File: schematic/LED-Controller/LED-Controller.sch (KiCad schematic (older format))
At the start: 17 parts

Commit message: Schematic first draft
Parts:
- removed J?: Enable Pull-ups, symbol Connector:Conn_01x02_Male
- removed R? (x5): R, symbol Device:R
- added D1: LED, LED_SMD:LED_0603_1608Metric_Pad1.05x0.95mm_HandSolder, symbol Device:LED
- added J10: String6, Connector_Wire:SolderWire-1sqmm_1x03_P7.8mm_D1.4mm_OD3.9mm, symbol Connector:Conn_01x03_Male
- added J3: RCin, Connector_PinHeader_2.54mm:PinHeader_1x03_P2.54mm_Horizontal, symbol Connector:Conn_01x03_Male
- added R1: 220, Resistor_SMD:R_0603_1608Metric, symbol Device:R
- added R2: 10k, Resistor_SMD:R_0603_1608Metric, symbol Device:R
- C1: renamed from C?; footprint (none) -> Capacitor_SMD:C_1206_3216Metric_Pad1.33x1.80mm_HandSolder
- C2: renamed from C?; value C -> 0.1 uF; footprint (none) -> Capacitor_SMD:C_0603_1608Metric_Pad1.08x0.95mm_HandSolder
- J1: renamed from J?; footprint (none) -> Connector_Wire:SolderWire-2.5sqmm_1x02_P8.8mm_D2.4mm_OD4.4mm
- J4: renamed from J?; footprint (none) -> Connector_PinHeader_2.54mm:PinHeader_1x03_P2.54mm_Vertical
- J5, J6, J7, J8, J9: renamed from J?; footprint (none) -> Connector_Wire:SolderWire-1sqmm_1x03_P7.8mm_D1.4mm_OD3.9mm
- U1: renamed from U?; value PIC18F26K22-xSO -> PIC18F27Q43-xSO
- gave numbers to parts that had none: 1
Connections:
- net GND: now also C2.1, J2.3 (Pin_3), J4.2 (Pin_2), U1.19 (VSS), U1.8 (VSS), J10.1 (Pin_1), J3.1 (Pin_1), R1.2
- net VDD: now also C2.2, J2.2 (Pin_2), U1.20 (VDD), J10.3 (Pin_3), R2.1
- net at J4.1 (Pin_1): now also U1.12 (RC1/SOSCI)
- net at J4.3 (Pin_3): now also U1.11 (RC0/SOSCO)
- net at J5.2 (Pin_2): now also U1.3 (RA1)
- net at J6.2 (Pin_2): now also U1.4 (RA2)
- net at J7.2 (Pin_2): now also U1.24 (RB3)
- net at J8.2 (Pin_2): now also U1.23 (RB2)
- net at J9.2 (Pin_2): now also U1.16 (RC5)
- net at U1.1 (~MCLR~/VPP/RE3): now also J2.1 (Pin_1), R2.2
- net at U1.13 (RC2): now also J3.3 (Pin_3)
- net at U1.17 (RC6): now also J10.2 (Pin_2)
- net at U1.27 (RB6/PGC): now also J2.5 (Pin_5)
- net at U1.28 (RB7/PGD): now also J2.4 (Pin_4)
- net at U1.9 (RA7/OSC1_CLKIN): now also D1.2 (A)
- new net: D1.1 (K), R1.1
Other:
- note added: "LED Strings"
- moved on the sheet: C2, J2, J4, U1

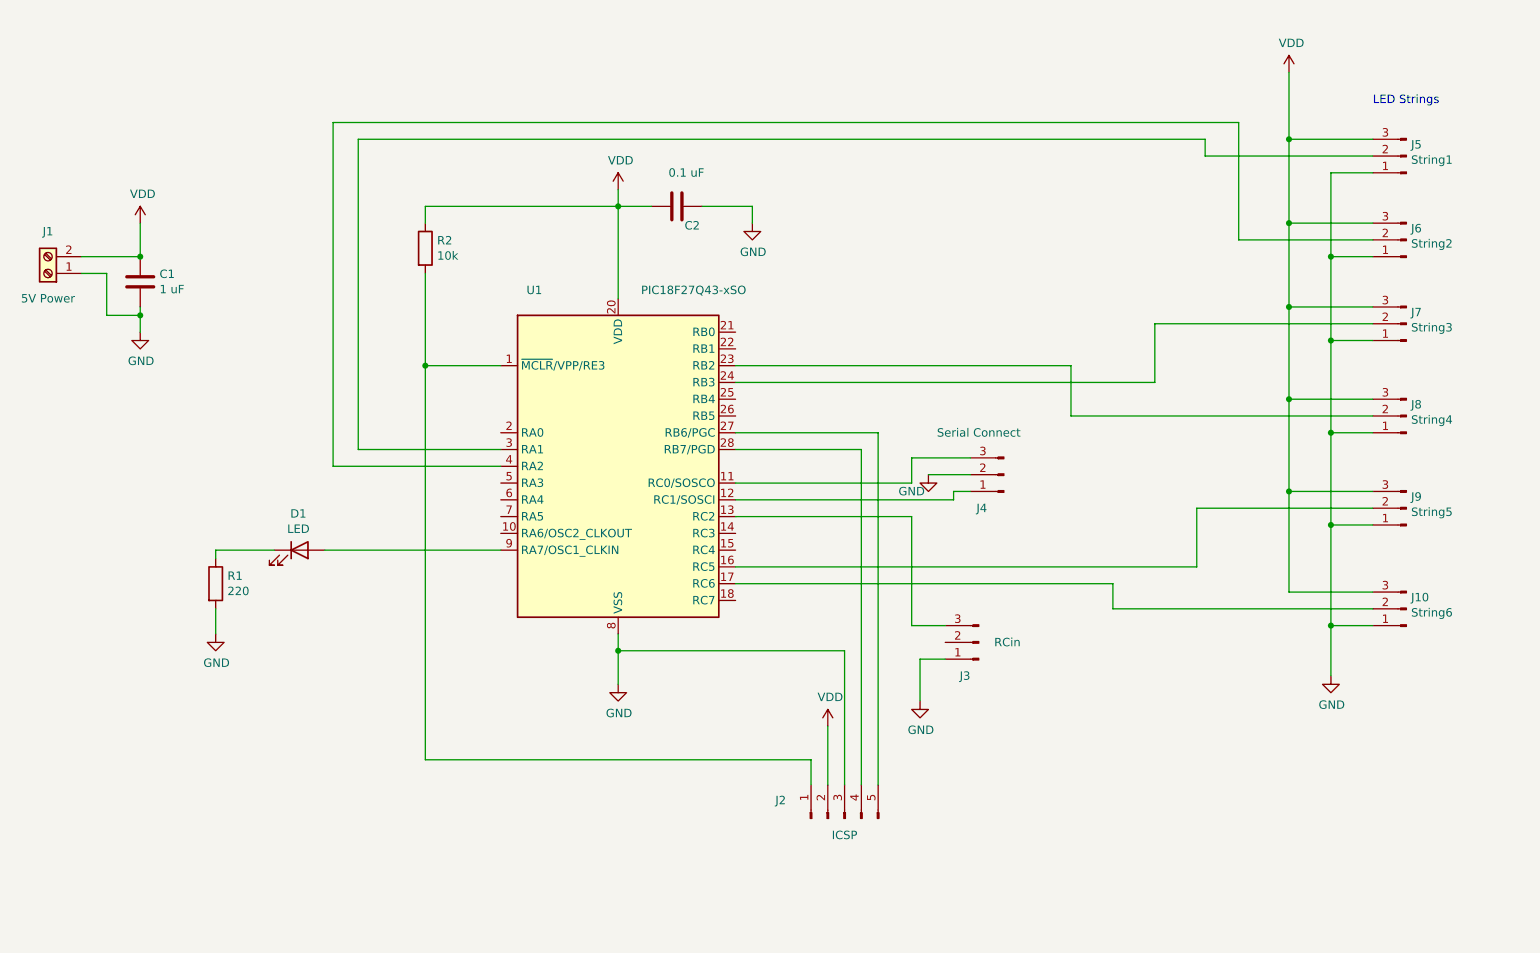
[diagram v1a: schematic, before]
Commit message: Initial pcb
Some schematic adjustments to improve pcb layout
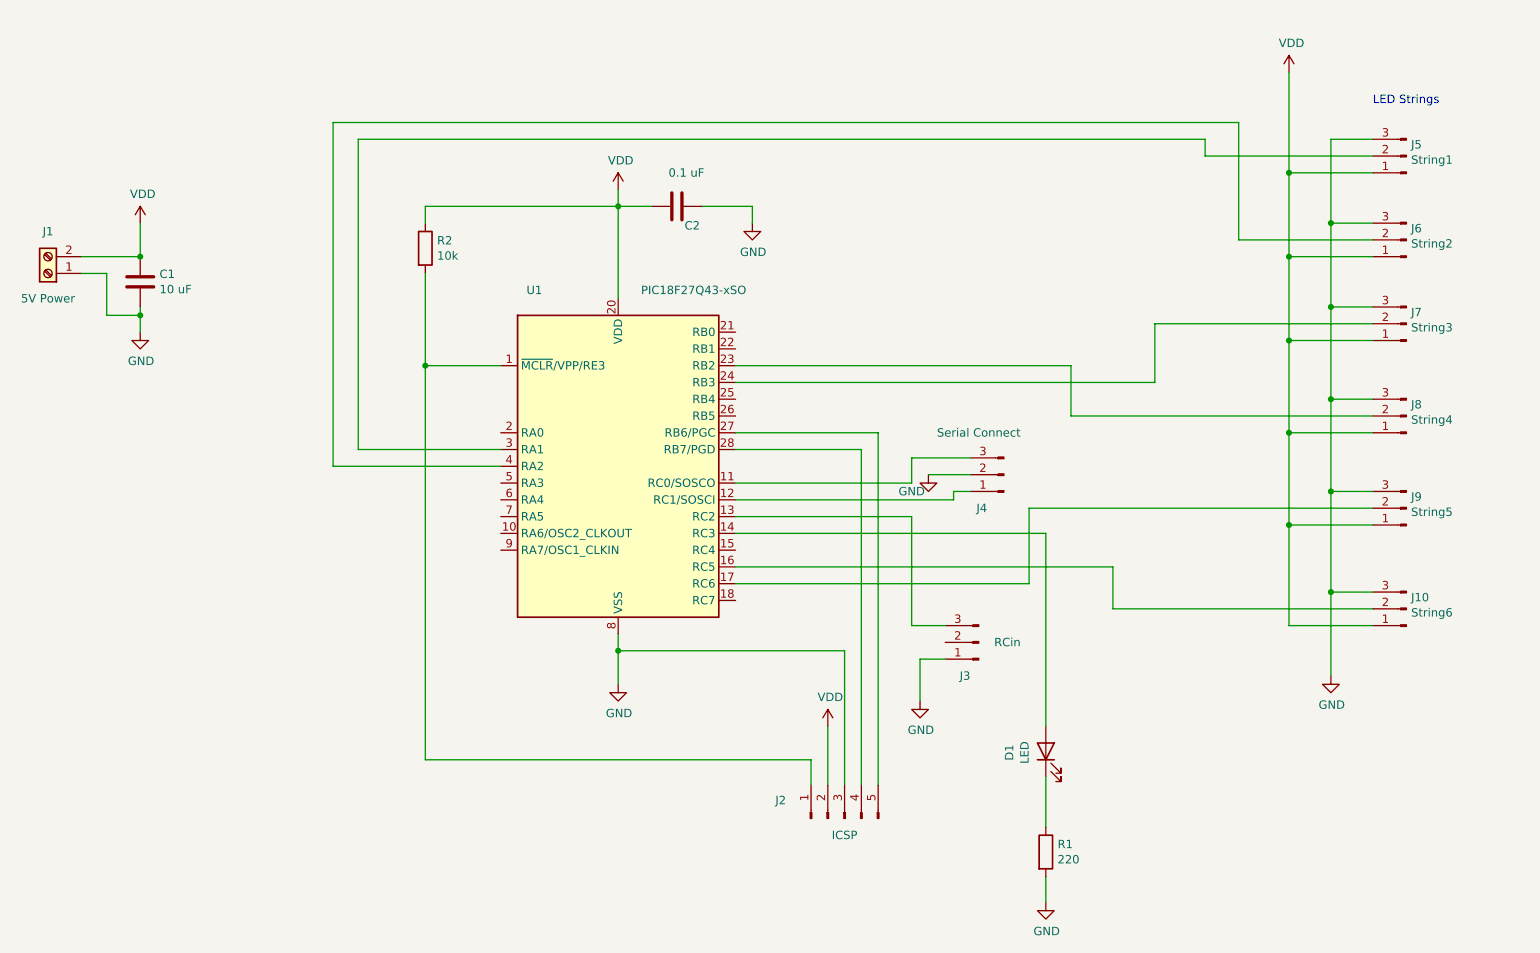
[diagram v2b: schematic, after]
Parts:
- C1: value 1 uF -> 10 uF
- J10, J5, J6, J7, J8, J9: footprint Connector_Wire:SolderWire-1sqmm_1x03_P7.8mm_D1.4mm_OD3.9mm -> LEDStringConn:TopBottom_3Pin
- J2: footprint (none) -> Connector_PinHeader_2.54mm:PinHeader_1x05_P2.54mm_Vertical
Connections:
- net GND: now also J10.3 (Pin_3), J5.3 (Pin_3), J6.3 (Pin_3), J7.3 (Pin_3), J8.3 (Pin_3), J9.3 (Pin_3); no longer J10.1 (Pin_1), J5.1 (Pin_1), J6.1 (Pin_1), J7.1 (Pin_1), J8.1 (Pin_1), J9.1 (Pin_1)
- net VDD: now also J10.1 (Pin_1), J5.1 (Pin_1), J6.1 (Pin_1), J7.1 (Pin_1), J8.1 (Pin_1), J9.1 (Pin_1); no longer J10.3 (Pin_3), J5.3 (Pin_3), J6.3 (Pin_3), J7.3 (Pin_3), J8.3 (Pin_3), J9.3 (Pin_3)
- net at J9.2 (Pin_2): now also U1.17 (RC6); no longer U1.16 (RC5)
- net at J10.2 (Pin_2): now also U1.16 (RC5); no longer U1.17 (RC6)
- net at U1.14 (RC3): now also D1.2 (A)
- net at U1.9 (RA7/OSC1_CLKIN): no longer D1.2 (A)
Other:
- moved on the sheet: D1, R1
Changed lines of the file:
@@
 P 1600 2450
 F 0 "C1" H 1715 2496 50  0000 L CNN
-F 1 "1 uF" H 1715 2405 50  0000 L CNN
+F 1 "10 uF" H 1715 2405 50  0000 L CNN
 F 2 "Capacitor_SMD:C_1206_3216Metric_Pad1.33x1.80mm_HandSolder" H 1638 2300 50  0001 C CNN
 F 3 "~" H 1600 2450 50  0001 C CNN
@@
 F 0 "J9" H 9122 3732 50  0000 R CNN
 F 1 "String5" H 9122 3823 50  0000 R CNN
-F 2 "Connector_Wire:SolderWire-1sqmm_1x03_P7.8mm_D1.4mm_OD3.9mm" H 9150 3800 50  0001 C CNN
+F 2 "LEDStringConn:TopBottom_3Pin" H 9150 3800 50  0001 C CNN
 F 3 "~" H 9150 3800 50  0001 C CNN
 	1    9150 3800
@@
 F 0 "J8" H 9122 3182 50  0000 R CNN
 F 1 "String4" H 9122 3273 50  0000 R CNN
-F 2 "Connector_Wire:SolderWire-1sqmm_1x03_P7.8mm_D1.4mm_OD3.9mm" H 9150 3250 50  0001 C CNN
+F 2 "LEDStringConn:TopBottom_3Pin" H 9150 3250 50  0001 C CNN
 F 3 "~" H 9150 3250 50  0001 C CNN
 	1    9150 3250
@@
 F 0 "J7" H 9122 2632 50  0000 R CNN
 F 1 "String3" H 9122 2723 50  0000 R CNN
-F 2 "Connector_Wire:SolderWire-1sqmm_1x03_P7.8mm_D1.4mm_OD3.9mm" H 9150 2700 50  0001 C CNN
+F 2 "LEDStringConn:TopBottom_3Pin" H 9150 2700 50  0001 C CNN
 F 3 "~" H 9150 2700 50  0001 C CNN
 	1    9150 2700
@@
 F 0 "J6" H 9122 2132 50  0000 R CNN
 F 1 "String2" H 9122 2223 50  0000 R CNN
-F 2 "Connector_Wire:SolderWire-1sqmm_1x03_P7.8mm_D1.4mm_OD3.9mm" H 9150 2200 50  0001 C CNN
+F 2 "LEDStringConn:TopBottom_3Pin" H 9150 2200 50  0001 C CNN
 F 3 "~" H 9150 2200 50  0001 C CNN
 	1    9150 2200
@@
 F 0 "J5" H 9122 1632 50  0000 R CNN
 F 1 "String1" H 9122 1723 50  0000 R CNN
-F 2 "Connector_Wire:SolderWire-1sqmm_1x03_P7.8mm_D1.4mm_OD3.9mm" H 9150 1700 50  0001 C CNN
+F 2 "LEDStringConn:TopBottom_3Pin" H 9150 1700 50  0001 C CNN
 F 3 "~" H 9150 1700 50  0001 C CNN
 	1    9150 1700
@@
 	1    0    0    -1
 $EndComp
-Wire Wire Line
-	8700 3900 8950 3900
-Wire Wire Line
-	8950 3350 8700 3350
-Wire Wire Line
-	8700 3350 8700 3900
-Connection ~ 8700 3900
-Wire Wire Line
-	8950 2800 8700 2800
-Wire Wire Line
-	8700 2800 8700 3350
-Connection ~ 8700 3350
-Wire Wire Line
-	8950 2300 8700 2300
-Wire Wire Line
-	8700 2300 8700 2800
-Connection ~ 8700 2800
-Wire Wire Line
-	8950 1800 8700 1800
-Wire Wire Line
-	8700 1800 8700 2300
-Connection ~ 8700 2300
-Wire Wire Line
-	8950 1600 8450 1600
-Wire Wire Line
-	8950 2100 8450 2100
-Wire Wire Line
-	8450 2100 8450 1600
-Connection ~ 8450 1600
-Wire Wire Line
-	8950 2600 8450 2600
-Wire Wire Line
-	8450 2600 8450 2100
-Connection ~ 8450 2100
-Wire Wire Line
-	8950 3150 8450 3150
-Wire Wire Line
-	8450 3150 8450 2600
-Connection ~ 8450 2600
-Wire Wire Line
-	8950 3700 8450 3700
-Wire Wire Line
-	8450 3700 8450 3150
-Connection ~ 8450 3150
 $Comp
 L Connector:Conn_01x05_Male J2
@@
 F 0 "J2" V 5908 6031 50  0000 C CNN
 F 1 "ICSP" V 5700 5650 50  0000 C CNN
-F 2 "" H 5800 5650 50  0001 C CNN
+F 2 "Connector_PinHeader_2.54mm:PinHeader_1x05_P2.54mm_Vertical" H 5800 5650 50  0001 C CNN
 F 3 "~" H 5800 5650 50  0001 C CNN
 	1    5800 5650
@@
 	-1   0    0    1
 $EndComp
-Wire Wire Line
-	8450 1200 8450 1600
 $Comp
 L Device:R R2
@@
 	7150 3250 8950 3250
 Wire Wire Line
-	5150 4150 7900 4150
-Wire Wire Line
-	7900 4150 7900 3800
-Wire Wire Line
-	7900 3800 8950 3800
-Wire Wire Line
 	5150 3750 6450 3750
 Wire Wire Line
@@
 F 0 "J10" H 9122 4332 50  0000 R CNN
 F 1 "String6" H 9122 4423 50  0000 R CNN
-F 2 "Connector_Wire:SolderWire-1sqmm_1x03_P7.8mm_D1.4mm_OD3.9mm" H 9150 4400 50  0001 C CNN
+F 2 "LEDStringConn:TopBottom_3Pin" H 9150 4400 50  0001 C CNN
 F 3 "~" H 9150 4400 50  0001 C CNN
 	1    9150 4400
@@
 $EndComp
 Wire Wire Line
-	8700 3900 8700 4500
-Wire Wire Line
-	8950 4500 8700 4500
-Connection ~ 8700 4500
-Wire Wire Line
-	8700 4500 8700 4800
-Wire Wire Line
-	8950 4300 8450 4300
-Wire Wire Line
-	8450 4300 8450 3700
-Connection ~ 8450 3700
-Wire Wire Line
 	8950 4400 7400 4400
-Wire Wire Line
-	7400 4400 7400 4250
-Wire Wire Line
-	7400 4250 5150 4250
 $Comp
 L Device:LED D1
 U 1 1 602B6ED3
-P 2550 4050
-F 0 "D1" H 2543 4267 50  0000 C CNN
-F 1 "LED" H 2543 4176 50  0000 C CNN
-F 2 "LED_SMD:LED_0603_1608Metric_Pad1.05x0.95mm_HandSolder" H 2550 4050 50  0001 C CNN
-F 3 "~" H 2550 4050 50  0001 C CNN
-	1    2550 4050
-	1    0    0    -1
+P 7000 5250
+F 0 "D1" H 6993 5467 50  0000 C CNN
+F 1 "LED" H 6993 5376 50  0000 C CNN
+F 2 "LED_SMD:LED_0603_1608Metric_Pad1.05x0.95mm_HandSolder" H 7000 5250 50  0001 C CNN
+F 3 "~" H 7000 5250 50  0001 C CNN
+	1    7000 5250
+	0    -1   -1   0
 $EndComp
 $Comp
 L Device:R R1
 U 1 1 602B7BC0
-P 2050 4250
-F 0 "R1" H 2120 4296 50  0000 L CNN
-F 1 "220" H 2120 4205 50  0000 L CNN
-F 2 "Resistor_SMD:R_0603_1608Metric" V 1980 4250 50  0001 C CNN
-F 3 "~" H 2050 4250 50  0001 C CNN
-	1    2050 4250
+P 7000 5850
+F 0 "R1" H 7070 5896 50  0000 L CNN
+F 1 "220" H 7070 5805 50  0000 L CNN
+F 2 "Resistor_SMD:R_0603_1608Metric" V 6930 5850 50  0001 C CNN
+F 3 "~" H 7000 5850 50  0001 C CNN
+	1    7000 5850
 	1    0    0    -1
 $EndComp
@@
 L power:GND #PWR03
 U 1 1 602B7F4F
-P 2050 4550
-F 0 "#PWR03" H 2050 4300 50  0001 C CNN
-F 1 "GND" H 2055 4377 50  0000 C CNN
-F 2 "" H 2050 4550 50  0001 C CNN
-F 3 "" H 2050 4550 50  0001 C CNN
-	1    2050 4550
-	1    0    0    -1
-$EndComp
-Wire Wire Line
-	3750 4050 2700 4050
-Wire Wire Line
-	2050 4550 2050 4400
-Wire Wire Line
-	2050 4100 2050 4050
-Wire Wire Line
-	2050 4050 2400 4050
+P 7000 6150
+F 0 "#PWR03" H 7000 5900 50  0001 C CNN
+F 1 "GND" H 7005 5977 50  0000 C CNN
+F 2 "" H 7000 6150 50  0001 C CNN
+F 3 "" H 7000 6150 50  0001 C CNN
+	1    7000 6150
+	1    0    0    -1
+$EndComp
+Wire Wire Line
+	7000 6150 7000 6000
 Text Notes 8950 1400 0    50   ~ 0
 LED Strings
+Wire Wire Line
+	8950 4300 8700 4300
+Connection ~ 8700 4300
+Wire Wire Line
+	8700 4300 8700 4800
+Wire Wire Line
+	8950 3700 8700 3700
+Connection ~ 8700 3700
+Wire Wire Line
+	8700 3700 8700 4300
+Wire Wire Line
+	8450 4500 8950 4500
+Wire Wire Line
+	8950 3900 8450 3900
+Connection ~ 8450 3900
+Wire Wire Line
+	8450 3900 8450 4500
+Wire Wire Line
+	8950 3350 8450 3350
+Connection ~ 8450 3350
+Wire Wire Line
+	8450 3350 8450 3900
+Wire Wire Line
+	8950 3150 8700 3150
+Connection ~ 8700 3150
+Wire Wire Line
+	8700 3150 8700 3700
+Wire Wire Line
+	8950 2800 8450 2800
+Connection ~ 8450 2800
+Wire Wire Line
+	8450 2800 8450 3350
+Wire Wire Line
+	8950 2600 8700 2600
+Connection ~ 8700 2600
+Wire Wire Line
+	8700 2600 8700 3150
+Wire Wire Line
+	8950 2300 8450 2300
+Connection ~ 8450 2300
+Wire Wire Line
+	8450 2300 8450 2800
+Wire Wire Line
+	8950 2100 8700 2100
+Connection ~ 8700 2100
+Wire Wire Line
+	8700 2100 8700 2600
+Wire Wire Line
+	8450 1200 8450 1800
+Wire Wire Line
+	8700 1600 8950 1600
+Wire Wire Line
+	8700 1600 8700 2100
+Wire Wire Line
+	8950 1800 8450 1800
+Connection ~ 8450 1800
+Wire Wire Line
+	8450 1800 8450 2300
+Wire Wire Line
+	6900 3800 6900 4250
+Wire Wire Line
+	6900 4250 5150 4250
+Wire Wire Line
+	6900 3800 8950 3800
+Wire Wire Line
+	5150 4150 7400 4150
+Wire Wire Line
+	7400 4150 7400 4400
+Wire Wire Line
+	5150 3950 7000 3950
+Wire Wire Line
+	7000 3950 7000 5100
+Wire Wire Line
+	7000 5400 7000 5700
 $EndSCHEMATC
